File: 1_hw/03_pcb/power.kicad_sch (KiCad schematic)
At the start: 63 parts, among them U1 TLV70333DBV, U2 TLV76133DCY, U3 TLV70333DBV, U4 LM3880MF-1AA, U5 TLV70312DBV, U6 TLV70325DBV, U7 TPS65131RGE, U8 TPD2E001DRL

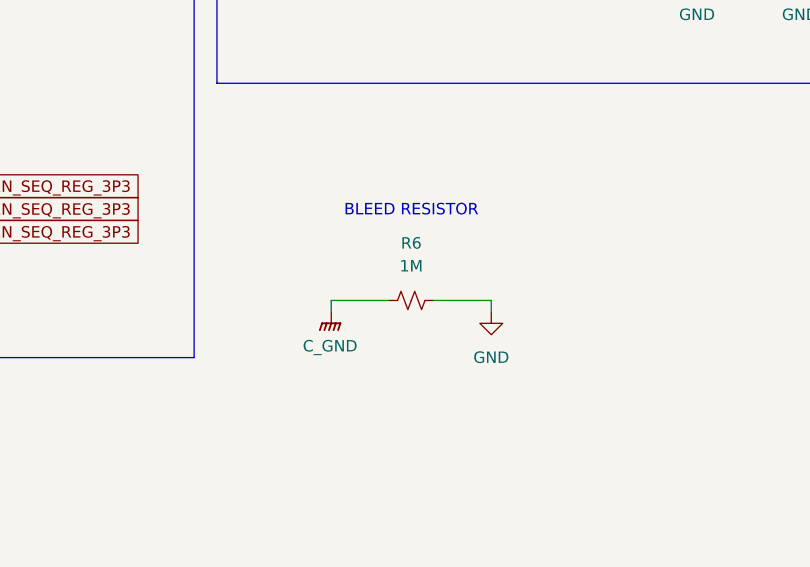
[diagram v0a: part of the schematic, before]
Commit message: FEAT: Removed Chassis GND, completed routing. Needs to be verified.
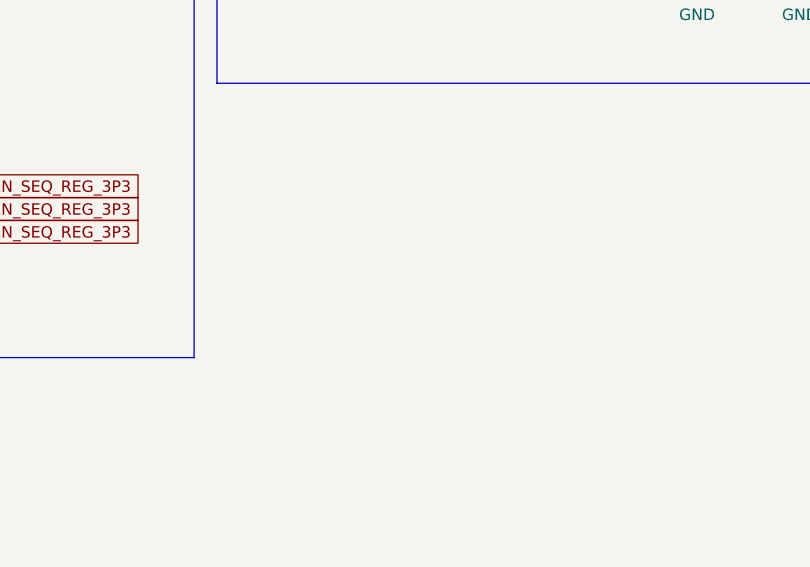
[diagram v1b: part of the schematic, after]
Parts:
- removed R6: 1M, Resistor_SMD:R_0603_1608Metric, symbol Device:R_Small_US
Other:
- note removed: "BLEED RESISTOR"
